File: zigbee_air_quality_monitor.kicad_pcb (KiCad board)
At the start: 4 copper layers, 19.8 x 50.9 mm, 38 parts, among them J1 USB_C_Receptacle_USB2.0, J2 QWIIC, J3 Conn_02x02_Odd_Even, SW1 PAIR_BTN, SW2 USER_BTN, U1 USBLC6-2SC6, U2 BT840, U3 XC6206P332MR, U4 SCD41-D-R2

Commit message: USB routing WIP
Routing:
- net /USB_CC1: track 0.00 -> 6.44 mm
- net /USB_CC2: track 0.00 -> 6.20 mm
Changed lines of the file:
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@@
   (gr_rect (start 122.1 89.2) (end 141.85 140.1)
     (stroke (width 0.1) (type default)) (fill none) (layer "Edge.Cuts"))
-  (segment (start 132.2 132.027499) (end 132.1475 131.974999) (width 0.23) (layer "F.Cu") (net 9))
-  (segment (start 131.04 134.525) (end 131.2 134.365) (width 0.23) (layer "F.Cu") (net 9))
+  (segment (start 129.124176 135.575) (end 125.8 135.575) (width 0.245) (layer "F.Cu") (net 8))
+  (segment (start 130.7 133.999176) (end 129.124176 135.575) (width 0.245) (layer "F.Cu") (net 8))
+  (segment (start 130.7 133.115) (end 130.7 133.999176) (width 0.245) (layer "F.Cu") (net 8))
   (segment (start 132.2 134.510956) (end 132.2 133.115) (width 0.23) (layer "F.Cu") (net 9))
-  (segment (start 132.875 130.7875) (end 132.875 130.425) (width 0.23) (layer "F.Cu") (net 9))
-  (segment (start 132.2 133.115) (end 132.2 132.027499) (width 0.23) (layer "F.Cu") (net 9))
-  (segment (start 132.54 131.306341) (end 132.54 131.1225) (width 0.23) (layer "F.Cu") (net 9))
-  (segment (start 132.1475 131.974999) (end 132.1475 131.698841) (width 0.23) (layer "F.Cu") (net 9))
-  (segment (start 131.2 134.365) (end 131.2 133.115) (width 0.23) (layer "F.Cu") (net 9))
+  (segment (start 132.875 131.175) (end 132.875 130.425) (width 0.23) (layer "F.Cu") (net 9))
+  (segment (start 131.2 134.450235) (end 131.2 133.115) (width 0.23) (layer "F.Cu") (net 9))
+  (segment (start 131.04 134.610235) (end 131.2 134.450235) (width 0.23) (layer "F.Cu") (net 9))
   (segment (start 132.299279 134.610235) (end 132.2 134.510956) (width 0.23) (layer "F.Cu") (net 9))
-  (segment (start 132.1475 131.698841) (end 132.54 131.306341) (width 0.23) (layer "F.Cu") (net 9))
-  (segment (start 132.54 131.1225) (end 132.875 130.7875) (width 0.23) (layer "F.Cu") (net 9))
-  (via (at 131.04 134.525) (size 0.7) (drill 0.3) (layers "F.Cu" "B.Cu") (net 9))
+  (segment (start 132.2 133.115) (end 132.2 131.85) (width 0.23) (layer "F.Cu") (net 9))
+  (segment (start 132.2 131.85) (end 132.875 131.175) (width 0.23) (layer "F.Cu") (net 9))
+  (via (at 131.04 134.610235) (size 0.7) (drill 0.3) (layers "F.Cu" "B.Cu") (net 9))
   (via (at 132.299279 134.610235) (size 0.7) (drill 0.3) (layers "F.Cu" "B.Cu") (net 9))
-  (segment (start 131.125235 134.610235) (end 132.299279 134.610235) (width 0.23) (layer "B.Cu") (net 9))
-  (segment (start 131.04 134.525) (end 131.125235 134.610235) (width 0.23) (layer "B.Cu") (net 9))
-  (segment (start 131.31 131.1225) (end 130.975 130.7875) (width 0.23) (layer "F.Cu") (net 10))
+  (segment (start 131.04 134.610235) (end 132.299279 134.610235) (width 0.23) (layer "B.Cu") (net 9))
+  (segment (start 130.975 131.1375) (end 130.975 130.425) (width 0.23) (layer "F.Cu") (net 10))
   (segment (start 132.004523 135.25) (end 132.6 135.25) (width 0.23) (layer "F.Cu") (net 10))
-  (segment (start 131.7275 131.551766) (end 131.31 131.134266) (width 0.23) (layer "F.Cu") (net 10))
   (segment (start 131.7 133.115) (end 131.67 133.145) (width 0.23) (layer "F.Cu") (net 10))
   (segment (start 132.95 134.37) (end 132.7 134.12) (width 0.23) (layer "F.Cu") (net 10))
@@
   (segment (start 132.6 135.25) (end 132.95 134.9) (width 0.23) (layer "F.Cu") (net 10))
   (segment (start 132.7 134.12) (end 132.7 133.115) (width 0.23) (layer "F.Cu") (net 10))
-  (segment (start 130.975 130.7875) (end 130.975 130.425) (width 0.23) (layer "F.Cu") (net 10))
-  (segment (start 131.7 133.115) (end 131.7 132.027499) (width 0.23) (layer "F.Cu") (net 10))
-  (segment (start 131.7525 131.974999) (end 131.7525 131.85) (width 0.23) (layer "F.Cu") (net 10))
   (segment (start 131.67 133.145) (end 131.67 134.915477) (width 0.23) (layer "F.Cu") (net 10))
-  (segment (start 131.7525 131.85) (end 131.7275 131.825) (width 0.23) (layer "F.Cu") (net 10))
-  (segment (start 131.7275 131.825) (end 131.7275 131.551766) (width 0.23) (layer "F.Cu") (net 10))
-  (segment (start 131.31 131.134266) (end 131.31 131.1225) (width 0.23) (layer "F.Cu") (net 10))
-  (segment (start 131.7 132.027499) (end 131.7525 131.974999) (width 0.23) (layer "F.Cu") (net 10))
-  (segment (start 131.578234 127.1725) (end 131.727499 127.1725) (width 0.23) (layer "F.Cu") (net 54))
+  (segment (start 131.7 131.8625) (end 130.975 131.1375) (width 0.23) (layer "F.Cu") (net 10))
+  (segment (start 131.7 133.115) (end 131.7 131.8625) (width 0.23) (layer "F.Cu") (net 10))
+  (segment (start 134.868586 135.575) (end 138.125 135.575) (width 0.245) (layer "F.Cu") (net 12))
+  (segment (start 133.7 134.406414) (end 134.868586 135.575) (width 0.245) (layer "F.Cu") (net 12))
+  (segment (start 133.7 133.115) (end 133.7 134.406414) (width 0.245) (layer "F.Cu") (net 12))
+  (segment (start 131.578234 127.001125) (end 131.4925 126.915391) (width 0.23) (layer "F.Cu") (net 54))
   (segment (start 135.79002 97) (end 135.84002 96.95) (width 0.23) (layer "F.Cu") (net 54))
   (segment (start 136.479216 95.964257) (end 136.244217 95.729258) (width 0.23) (layer "F.Cu") (net 54))
-  (segment (start 131.727499 127.15039) (end 131.4925 126.915391) (width 0.23) (layer "F.Cu") (net 54))
   (segment (start 136.457415 95.964257) (end 136.479216 95.964257) (width 0.23) (layer "F.Cu") (net 54))
-  (segment (start 131.31 127.815) (end 131.31 127.440734) (width 0.23) (layer "F.Cu") (net 54))
-  (segment (start 131.31 127.440734) (end 131.578234 127.1725) (width 0.23) (layer "F.Cu") (net 54))
+  (segment (start 130.975 127.775734) (end 131.578234 127.1725) (width 0.23) (layer "F.Cu") (net 54))
   (segment (start 135.84002 96.95) (end 135.84002 96.581652) (width 0.23) (layer "F.Cu") (net 54))
+  (segment (start 130.975 128.15) (end 130.975 127.775734) (width 0.23) (layer "F.Cu") (net 54))
   (segment (start 135.84002 96.581652) (end 136.457415 95.964257) (width 0.23) (layer "F.Cu") (net 54))
-  (segment (start 130.975 128.15) (end 131.31 127.815) (width 0.23) (layer "F.Cu") (net 54))
   (segment (start 135.35 97) (end 135.79002 97) (width 0.23) (layer "F.Cu") (net 54))
-  (segment (start 131.727499 127.1725) (end 131.727499 127.15039) (width 0.23) (layer "F.Cu") (net 54))
+  (segment (start 131.578234 127.1725) (end 131.578234 127.001125) (width 0.23) (layer "F.Cu") (net 54))
   (via (at 131.4925 126.915391) (size 0.7) (drill 0.3) (layers "F.Cu" "B.Cu") (net 54))
   (via (at 136.244217 95.729258) (size 0.7) (drill 0.3) (layers "F.Cu" "B.Cu") (net 54))
@@
   (segment (start 134.1525 124.255391) (end 132.1225 126.285391) (width 0.23) (layer "B.Cu") (net 54))
   (segment (start 136.479217 95.964258) (end 136.479217 100.291475) (width 0.23) (layer "B.Cu") (net 54))
+  (segment (start 132.875 127.775734) (end 132.3575 127.258234) (width 0.23) (layer "F.Cu") (net 55))
   (segment (start 135.35 98.2) (end 136.235 97.315) (width 0.23) (layer "F.Cu") (net 55))
+  (segment (start 132.3575 127.258234) (end 132.3575 126.915391) (width 0.23) (layer "F.Cu") (net 55))
   (segment (start 136.874218 95.964257) (end 137.109217 95.729258) (width 0.23) (layer "F.Cu") (net 55))
   (segment (start 136.595258 96.385) (end 136.874218 96.385) (width 0.23) (layer "F.Cu") (net 55))
-  (segment (start 132.54 127.815) (end 132.54 127.440734) (width 0.23) (layer "F.Cu") (net 55))
   (segment (start 136.874218 96.385) (end 136.874218 95.964257) (width 0.23) (layer "F.Cu") (net 55))
-  (segment (start 132.122501 127.1725) (end 132.122501 127.15039) (width 0.23) (layer "F.Cu") (net 55))
-  (segment (start 132.875 128.15) (end 132.54 127.815) (width 0.23) (layer "F.Cu") (net 55))
-  (segment (start 132.54 127.440734) (end 132.271766 127.1725) (width 0.23) (layer "F.Cu") (net 55))
   (segment (start 136.235 96.745258) (end 136.595258 96.385) (width 0.23) (layer "F.Cu") (net 55))
-  (segment (start 132.271766 127.1725) (end 132.122501 127.1725) (width 0.23) (layer "F.Cu") (net 55))
-  (segment (start 132.122501 127.15039) (end 132.3575 126.915391) (width 0.23) (layer "F.Cu") (net 55))
+  (segment (start 132.875 128.15) (end 132.875 127.775734) (width 0.23) (layer "F.Cu") (net 55))
   (segment (start 136.235 97.315) (end 136.235 96.745258) (width 0.23) (layer "F.Cu") (net 55))
   (via (at 132.3575 126.915391) (size 0.7) (drill 0.3) (layers "F.Cu" "B.Cu") (net 55))

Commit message: All parts routed
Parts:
- moved D3 2.03 mm to (131.7, 102.0)
- moved kibuzzard-63D64589 2.02 mm to (131.8, 105.2)
- moved C4 0.26 mm to (140.7, 98.3)
- turned FB1 to -90 degrees
- turned R6 to -90 degrees
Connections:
- C1 pad 1: Net-(U2-P0.02/AIN0) -> Net-(U2-P0.09/NFC1)
- C2 pad 1: Net-(U2-P0.03/AIN1) -> Net-(U2-P0.10/NFC2)
- SW1 pad 1: Net-(U2-P0.02/AIN0) -> Net-(U2-P0.09/NFC1)
- SW2 pad 1: Net-(U2-P0.03/AIN1) -> Net-(U2-P0.10/NFC2)
- U2 pad 14: /PAIRING_LED -> unconnected-(U2-P0.18/RESET-Pad14)
- U2 pad 5: Net-(U2-P0.02/AIN0) -> /PAIRING_LED
- U2 pad 6: Net-(U2-P0.03/AIN1) -> unconnected-(U2-P0.03/AIN1-Pad6)
- U2 pad 7: unconnected-(U2-P0.09/NFC1-Pad7) -> Net-(U2-P0.09/NFC1)
- U2 pad 8: unconnected-(U2-P0.10/NFC2-Pad8) -> Net-(U2-P0.10/NFC2)
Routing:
- net +3.3V: track 0.00 -> 78.6 mm
- net VCC: track 0.00 -> 61.7 mm, vias 0 -> 5
- net Net-(U2-P0.10/NFC2): track 0.00 -> 40.6 mm, vias 0 -> 4
- net Net-(U2-P0.09/NFC1): track 0.00 -> 36.6 mm, vias 0 -> 2
- net /I2C_SCL: track 0.00 -> 29.1 mm, vias 0 -> 2
- net /I2C_SDA: track 0.00 -> 28.2 mm, vias 0 -> 3
- net /STATUS_LED: track 0.00 -> 23.3 mm, vias 0 -> 2
- net /PAIRING_LED: track 0.00 -> 21.9 mm, vias 0 -> 2
- net /SWCLK: track 0.00 -> 15.8 mm, vias 0 -> 1
- net /SWDIO: track 0.00 -> 15.2 mm, vias 0 -> 1
- net /AIR_QUALITY_LED: track 0.00 -> 12.8 mm
- net /USB_FUSE: track 0.00 -> 8.98 mm, vias 0 -> 2
- net VBUS: track 0.00 -> 6.20 mm
- net GND: track 0.00 -> 3.80 mm, vias 0 -> 1
- net Net-(D2-A): track 0.00 -> 1.41 mm
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
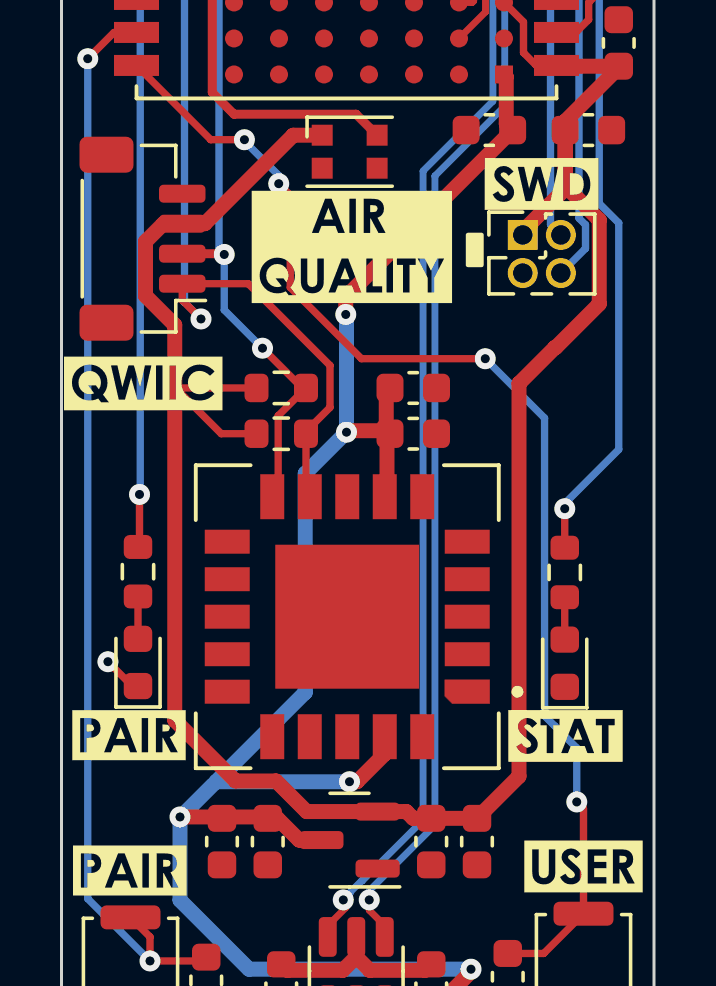
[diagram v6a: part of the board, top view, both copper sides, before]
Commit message: Added level translator for SCD40
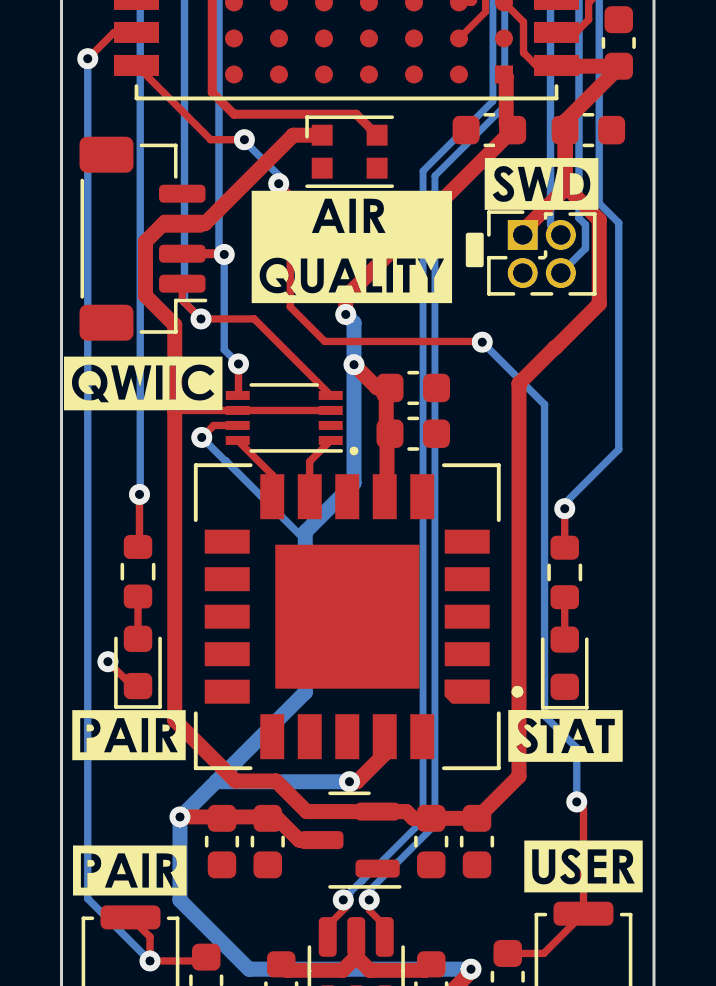
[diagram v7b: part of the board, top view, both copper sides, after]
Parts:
- removed R3, R4: 5k1, Resistor_SMD:R_0603_1608Metric
- added U6: TXS0102DCU, Package_SO:VSSOP-8_2.3x2mm_P0.5mm, F.Cu at (129.5, 110.8)
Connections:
- net Net-(U2-P0.09/NFC1) renamed /PAIR_BTN
- net Net-(U2-P0.10/NFC2) renamed /USER_BTN
- J2 pad 1: /I2C_SCL -> /I2C_SCL_3V3
- J2 pad 2: /I2C_SDA -> /I2C_SDA_3V3
- U2 pad 1: /I2C_SDA -> /I2C_SDA_3V3
- U2 pad 2: /I2C_SCL -> /I2C_SCL_3V3
- U4 pad 10: /I2C_SDA -> /I2C_SDA_5V
- U4 pad 9: /I2C_SCL -> /I2C_SCL_5V
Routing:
- net /I2C_SCL: track 29.1 -> 0.00 mm, vias 2 -> 0
- net /I2C_SDA: track 28.2 -> 0.00 mm, vias 3 -> 0
- net /I2C_SCL_3V3: track 0.00 -> 23.7 mm, vias 0 -> 2
- net /I2C_SDA_3V3: track 0.00 -> 23.3 mm, vias 0 -> 3
- net VCC: track 61.7 -> 68.5 mm, vias 5 -> 6
- net /I2C_SDA_5V: track 0.00 -> 2.63 mm
- net /I2C_SCL_5V: track 0.00 -> 2.16 mm
- net +3.3V: track 78.6 -> 77.8 mm
- net /USER_BTN: track 40.6 -> 41.2 mm
